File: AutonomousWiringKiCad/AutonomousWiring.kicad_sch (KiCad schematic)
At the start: 30 parts

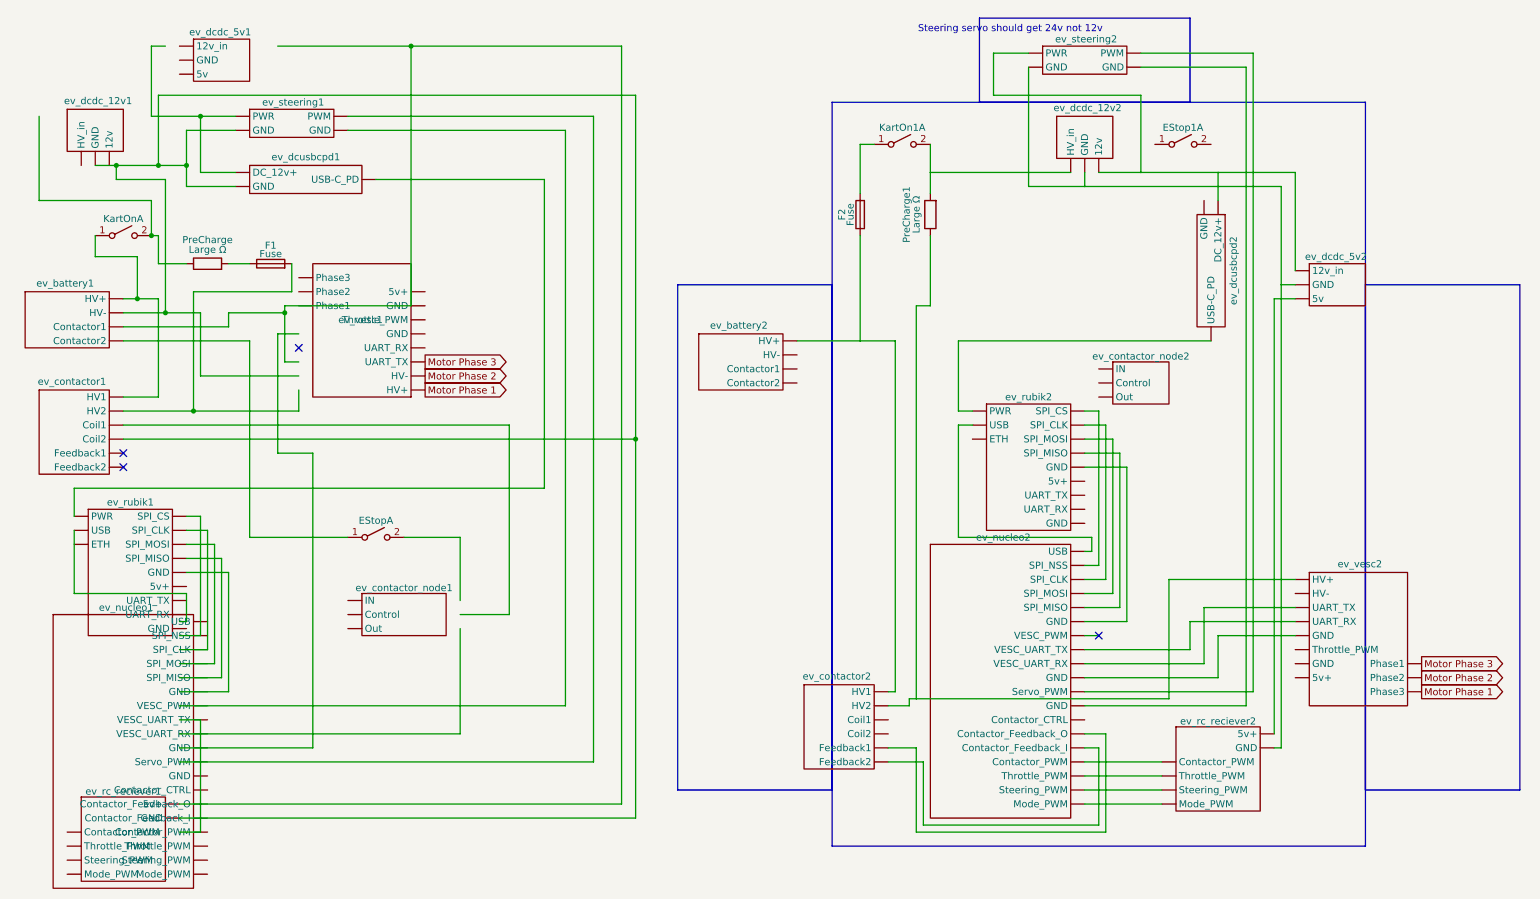
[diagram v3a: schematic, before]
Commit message: Not perfect but all wires in
- Servo needs 24v
- Missing bullet AC (24v passive PoE)
- Missing eth switch
- Missing 4 other rubiks
- Missing purely electrical remote contactor shutoff
- Don't use relay for STM set contactor
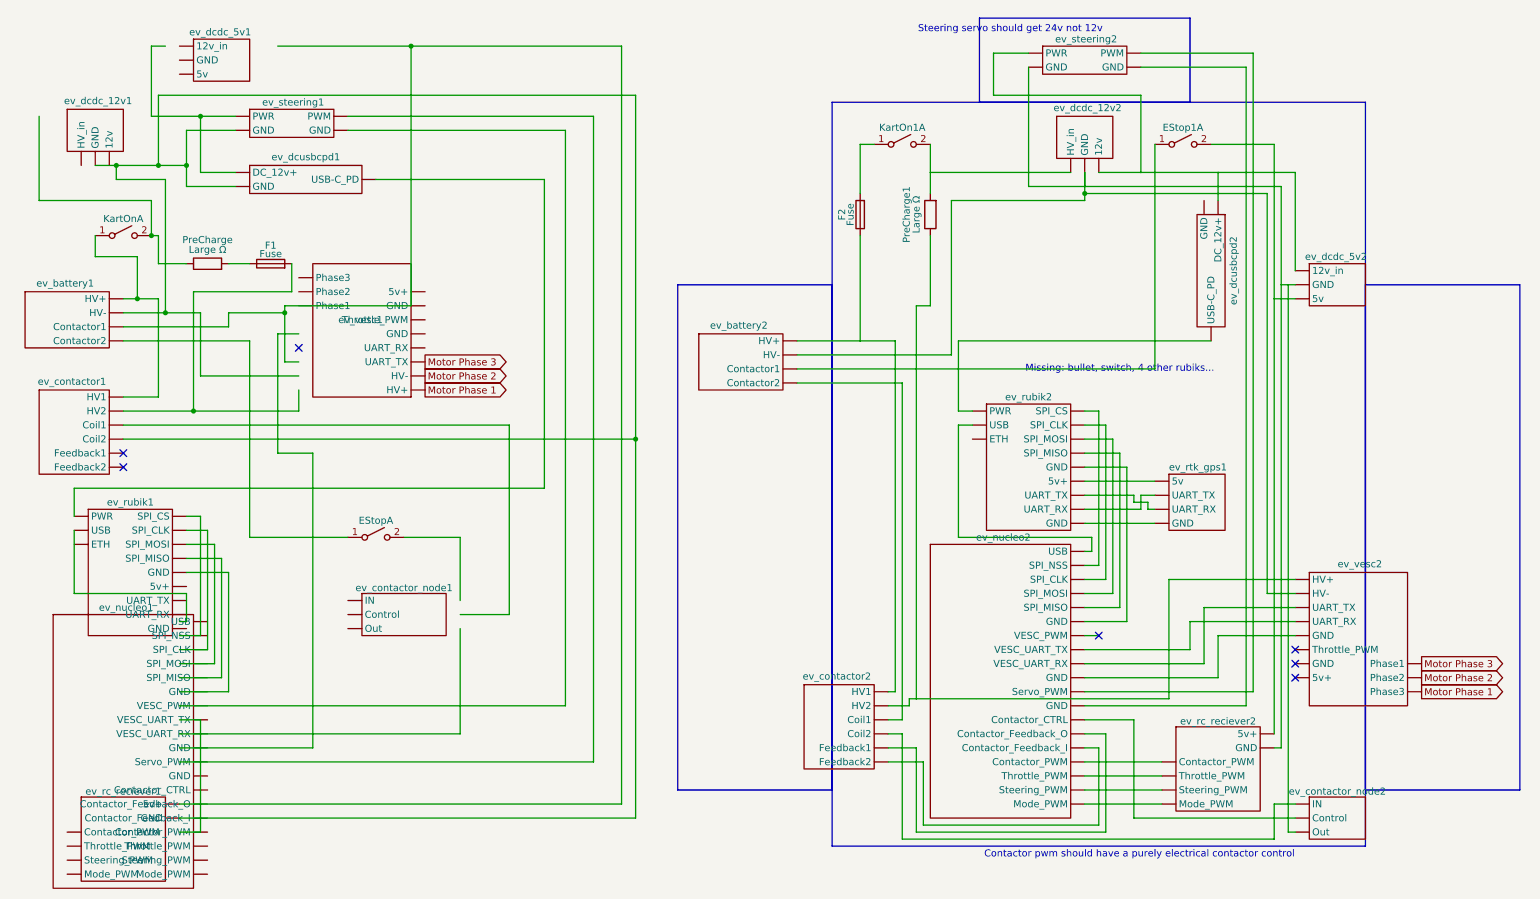
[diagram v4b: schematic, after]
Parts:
- added ev_rtk_gps1: ~, symbol ev_kart:ev_rtk_gps
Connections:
- net at ev_dcdc_12v1. (12v): now also ev_battery1. (Contactor2), ev_contactor1. (Feedback2), ev_dcusbcpd1. (USB-C_PD), ev_rc_reciever1. (GND), ev_steering1. (GND)
- net at ev_battery1. (Contactor2): now also EStop.1 (A); no longer ev_rc_reciever1. (GND)
- net at ev_nucleo2. (Mode_PWM): now also ev_vesc2. (Phase3)
- net at ev_steering2. (GND): now also ev_dcdc_12v2. (12v), ev_dcdc_5v2. (5v), ev_dcusbcpd2. (USB-C_PD); no longer ev_nucleo2. (Mode_PWM)
- net at ev_contactor2. (Feedback2): now also PreCharge1.1, ev_vesc2. (Phase3); no longer ev_nucleo2. (Mode_PWM)
- net at ev_rc_reciever2. (GND): now also EStop1.2 (B), ev_dcdc_5v2. (5v); no longer ev_nucleo2. (Mode_PWM)
- net at ev_rubik2. (GND): no longer ev_nucleo2. (Mode_PWM)
- net at ev_contactor_node2. (Out): now also ev_contactor2. (Feedback2)
- net at ev_battery2. (Contactor2): now also EStop1.1 (A)
- net at ev_steering1. (GND): now also ev_dcusbcpd1. (USB-C_PD)
- net at ev_dcusbcpd1. (USB-C_PD): now also ev_rubik1. (GND); no longer ev_steering1. (GND)
- net at ev_nucleo1. (Mode_PWM): now also ev_rubik1. (GND)
- net at ev_dcusbcpd2. (USB-C_PD): now also ev_rubik2. (GND)
- new net: ev_battery1. (Contactor2), ev_rc_reciever1. (GND)
- new net: KartOn.1 (A), ev_battery1. (Contactor2), ev_contactor1. (Feedback2)
- new net: ev_contactor_node2. (Out), ev_nucleo2. (Mode_PWM)
- new net: ev_nucleo2. (Mode_PWM), ev_steering2. (GND) (x2)
- new net: ev_contactor2. (Feedback2), ev_nucleo2. (Mode_PWM) (x2)
- new net: ev_nucleo2. (Mode_PWM), ev_rc_reciever2. (GND) (x4)
- new net: ev_nucleo2. (Mode_PWM), ev_rubik2. (GND) (x6)
- new net: ev_nucleo2. (Mode_PWM), ev_vesc2. (Phase3) (x2)
- new net: F2.1, ev_battery2. (Contactor2), ev_contactor2. (Feedback2)
- new net: ev_battery2. (Contactor2), ev_contactor_node2. (Out), ev_dcdc_12v2. (12v), ev_dcdc_5v2. (5v), ev_rc_reciever2. (GND), ev_steering2. (GND), ev_vesc2. (Phase3)
- new net: ev_battery2. (Contactor2), ev_contactor2. (Feedback2)
- new net: ev_rtk_gps1. (GND), ev_rubik2. (GND) (x4)
- now unconnected: ev_contactor1. (Feedback2), ev_contactor1. (Feedback2), ev_rc_reciever1. (GND), ev_rubik2. (GND), ev_rubik2. (GND), ev_rubik2. (GND), ev_rubik2. (GND), ev_rubik2. (GND), ev_rubik2. (GND)
- no-connect marks 4 -> 7
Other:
- note added: "Contactor pwm should have a purely electrical contactor control"
- note added: "Missing: bullet, switch, 4 other rubiks..."
- moved on the sheet: ev_contactor_node2

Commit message: Removing old draft
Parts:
- removed EStop, KartOn: SW_DPST_x2, symbol Switch:SW_DPST_x2
- removed F1: Fuse, symbol Device:Fuse
- removed PreCharge: Large Ω, symbol Device:R
- removed ev_battery1: ~, symbol ev_kart:ev_battery
- removed ev_contactor1: ~, symbol ev_kart:ev_contactor
- removed ev_contactor_node1: ~, symbol ev_kart:ev_contactor_node
- removed ev_dcdc_12v1: ~, symbol ev_kart:ev_dcdc_12v
- removed ev_dcdc_5v1: ~, symbol ev_kart:ev_dcdc_5v
- removed ev_dcusbcpd1: ~, symbol ev_kart:ev_dcusbcpd
- removed ev_nucleo1: ~, symbol ev_kart:ev_nucleo
- removed ev_rc_reciever1: ~, symbol ev_kart:ev_rc_reciever
- removed ev_rubik1: ~, symbol ev_kart:ev_rubik
- removed ev_steering1: ~, symbol ev_kart:ev_steering
- removed ev_vesc1: ~, symbol ev_kart:ev_vesc
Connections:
- net at ev_nucleo2. (Mode_PWM): now also ev_vesc2. (Phase3)
- net at ev_contactor_node2. (Out): now also ev_contactor2. (Feedback2); no longer ev_nucleo2. (Mode_PWM)
- net at ev_steering2. (GND): now also ev_dcdc_12v2. (12v), ev_dcdc_5v2. (5v), ev_dcusbcpd2. (USB-C_PD); no longer ev_nucleo2. (Mode_PWM)
- net at ev_contactor2. (Feedback2): now also PreCharge1.1, ev_vesc2. (Phase3); no longer ev_nucleo2. (Mode_PWM)
- net at ev_rc_reciever2. (GND): now also EStop1.2 (B), ev_dcdc_5v2. (5v); no longer ev_nucleo2. (Mode_PWM)
- net at ev_rubik2. (GND): no longer ev_nucleo2. (Mode_PWM)
- net at ev_battery2. (Contactor2): now also EStop1.1 (A); no longer ev_contactor2. (Feedback2)
- net at ev_dcusbcpd2. (USB-C_PD): now also ev_rubik2. (GND)
- new net: ev_contactor_node2. (Out), ev_nucleo2. (Mode_PWM)
- new net: ev_nucleo2. (Mode_PWM), ev_steering2. (GND) (x2)
- new net: ev_contactor2. (Feedback2), ev_nucleo2. (Mode_PWM) (x2)
- new net: ev_nucleo2. (Mode_PWM), ev_rc_reciever2. (GND) (x4)
- new net: ev_nucleo2. (Mode_PWM), ev_rubik2. (GND) (x6)
- new net: ev_nucleo2. (Mode_PWM), ev_vesc2. (Phase3) (x2)
- new net: F2.1, ev_battery2. (Contactor2), ev_contactor2. (Feedback2)
- new net: ev_battery2. (Contactor2), ev_contactor_node2. (Out), ev_dcdc_12v2. (12v), ev_dcdc_5v2. (5v), ev_rc_reciever2. (GND), ev_steering2. (GND), ev_vesc2. (Phase3)
- new net: ev_battery2. (Contactor2), ev_contactor2. (Feedback2)
- new net: ev_rtk_gps1. (GND), ev_rubik2. (GND) (x3)
- now unconnected: ev_rubik2. (GND), ev_rubik2. (GND), ev_rubik2. (GND), ev_rubik2. (GND), ev_rubik2. (GND), ev_rubik2. (GND), ev_rubik2. (GND), ev_rubik2. (GND), ev_rubik2. (GND)
- no-connect marks 7 -> 4
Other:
- moved on the sheet: EStop1A, F2, KartOn1A, PreCharge1, ev_battery2, ev_contactor2, ev_contactor_node2, ev_dcdc_12v2, ev_dcdc_5v2, ev_dcusbcpd2, ev_nucleo2, ev_rc_reciever2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

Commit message: Swapping 12v to 24v, placing eth setup on the side
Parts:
- removed ev_dcdc_12v2: ~, symbol ev_kart:ev_dcdc_12v
- added ev_bullet1: ~, symbol ev_kart:ev_bullet
- added ev_dcdc_24v1: ~, symbol ev_kart:ev_dcdc_24v
- added ev_eth_switch1: ~, symbol ev_kart:ev_eth_switch
- added ev_poe_adp1: ~, symbol ev_kart:ev_poe_adp
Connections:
- net at KartOn1.2 (B), PreCharge1.2: now also ev_dcdc_24v1. (24v)
- net at ev_nucleo2. (Mode_PWM): now also ev_vesc2. (Phase3)
- net at ev_contactor_node2. (Out): now also ev_contactor2. (Feedback2); no longer ev_nucleo2. (Mode_PWM)
- net at ev_contactor2. (Feedback2): now also PreCharge1.1, ev_vesc2. (Phase3); no longer ev_nucleo2. (Mode_PWM)
- net at ev_rc_reciever2. (GND): now also EStop1.2 (B), ev_dcdc_5v2. (5v); no longer ev_nucleo2. (Mode_PWM)
- net Eth Switch: now reaches ev_rubik2. (GND)
- net Eth Switch: no longer ev_nucleo2. (Mode_PWM)
- net at ev_battery2. (Contactor2): now also EStop1.1 (A); no longer ev_contactor2. (Feedback2)
- net at ev_dcusbcpd2. (USB-C_PD): now also ev_rubik2. (GND)
- new net: ev_battery2. (Contactor2), ev_contactor_node2. (Out), ev_dcdc_24v1. (24v), ev_dcdc_5v2. (5v), ev_rc_reciever2. (GND), ev_steering2. (GND), ev_vesc2. (Phase3)
- new net: ev_dcdc_24v1. (24v), ev_dcdc_5v2. (5v), ev_dcusbcpd2. (USB-C_PD), ev_steering2. (GND)
- new net: ev_contactor_node2. (Out), ev_nucleo2. (Mode_PWM)
- new net: ev_nucleo2. (Mode_PWM), ev_steering2. (GND)
- new net: ev_contactor2. (Feedback2), ev_nucleo2. (Mode_PWM) (x2)
- new net: ev_nucleo2. (Mode_PWM), ev_rc_reciever2. (GND) (x4)
- new net: ev_nucleo2. (Mode_PWM), ev_rubik2. (GND) (x6)
- new net: ev_nucleo2. (Mode_PWM), ev_vesc2. (Phase3) (x2)
- new net: F2.1, ev_battery2. (Contactor2), ev_contactor2. (Feedback2)
- new net: ev_eth_switch1. (ETH6), ev_poe_adp1. (POE_Eth) (x2)
- new net: ev_bullet1. (PoE_Eth), ev_poe_adp1. (POE_Eth)
- new net: ev_battery2. (Contactor2), ev_contactor2. (Feedback2)
- new net: ev_rtk_gps1. (GND), ev_rubik2. (GND) (x3)
- new net Rubik 1: ev_eth_switch1. (ETH6)
- new net Rubik 2: ev_eth_switch1. (ETH6)
- new net Rubik 3: ev_eth_switch1. (ETH6)
- new net Rubik 4: ev_eth_switch1. (ETH6)
- new net Rubik 5: ev_eth_switch1. (ETH6)
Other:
- note removed: "Steering servo should get 24v not 12v"

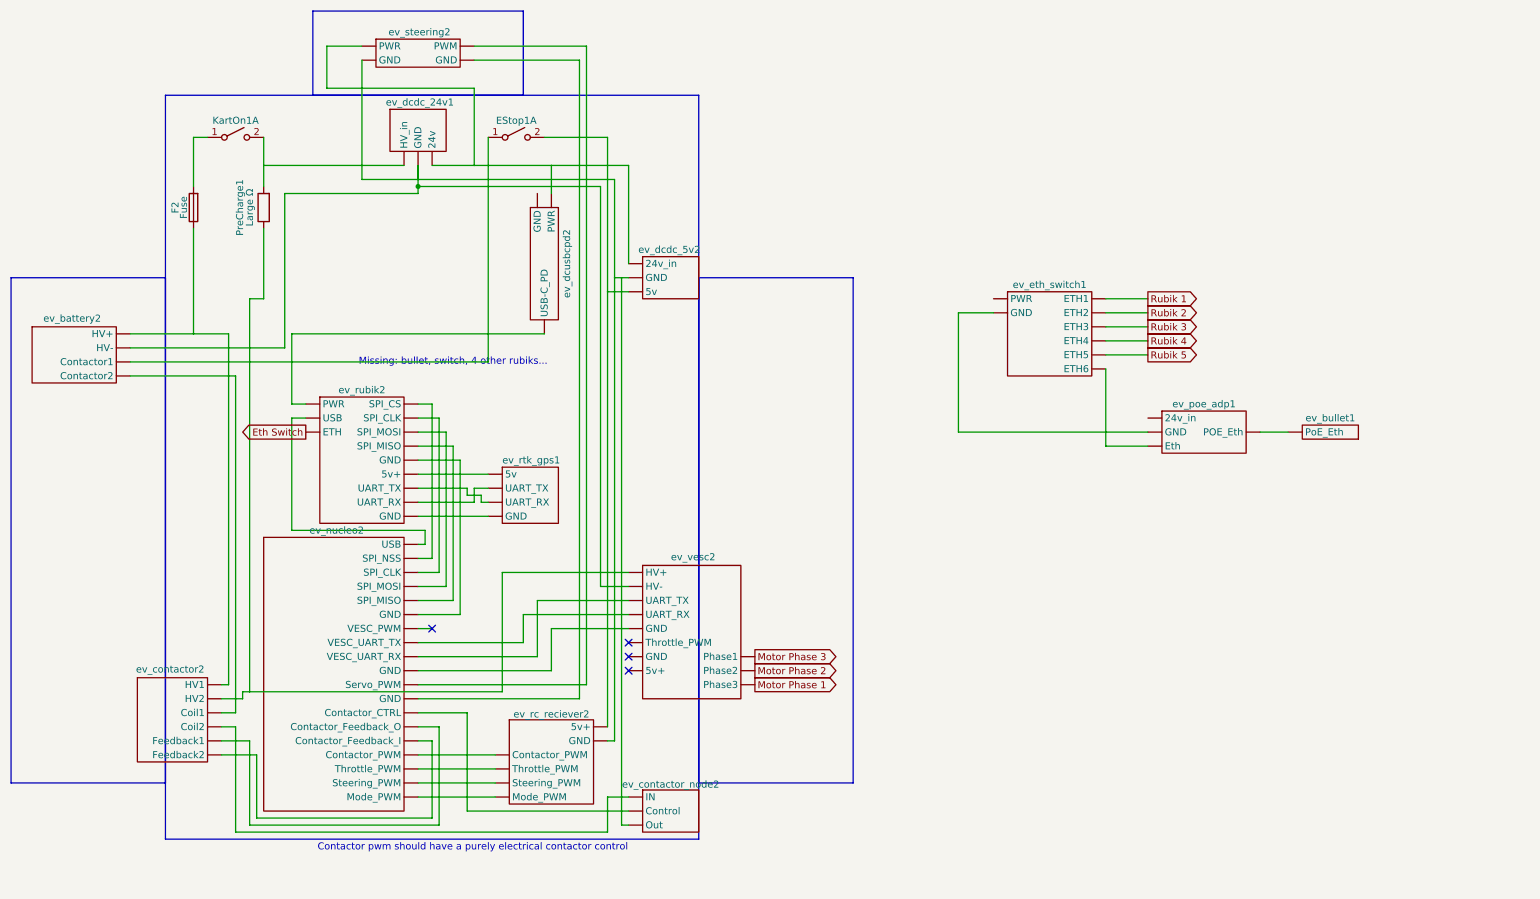
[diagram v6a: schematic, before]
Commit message: Moving eth setup into the main diagram
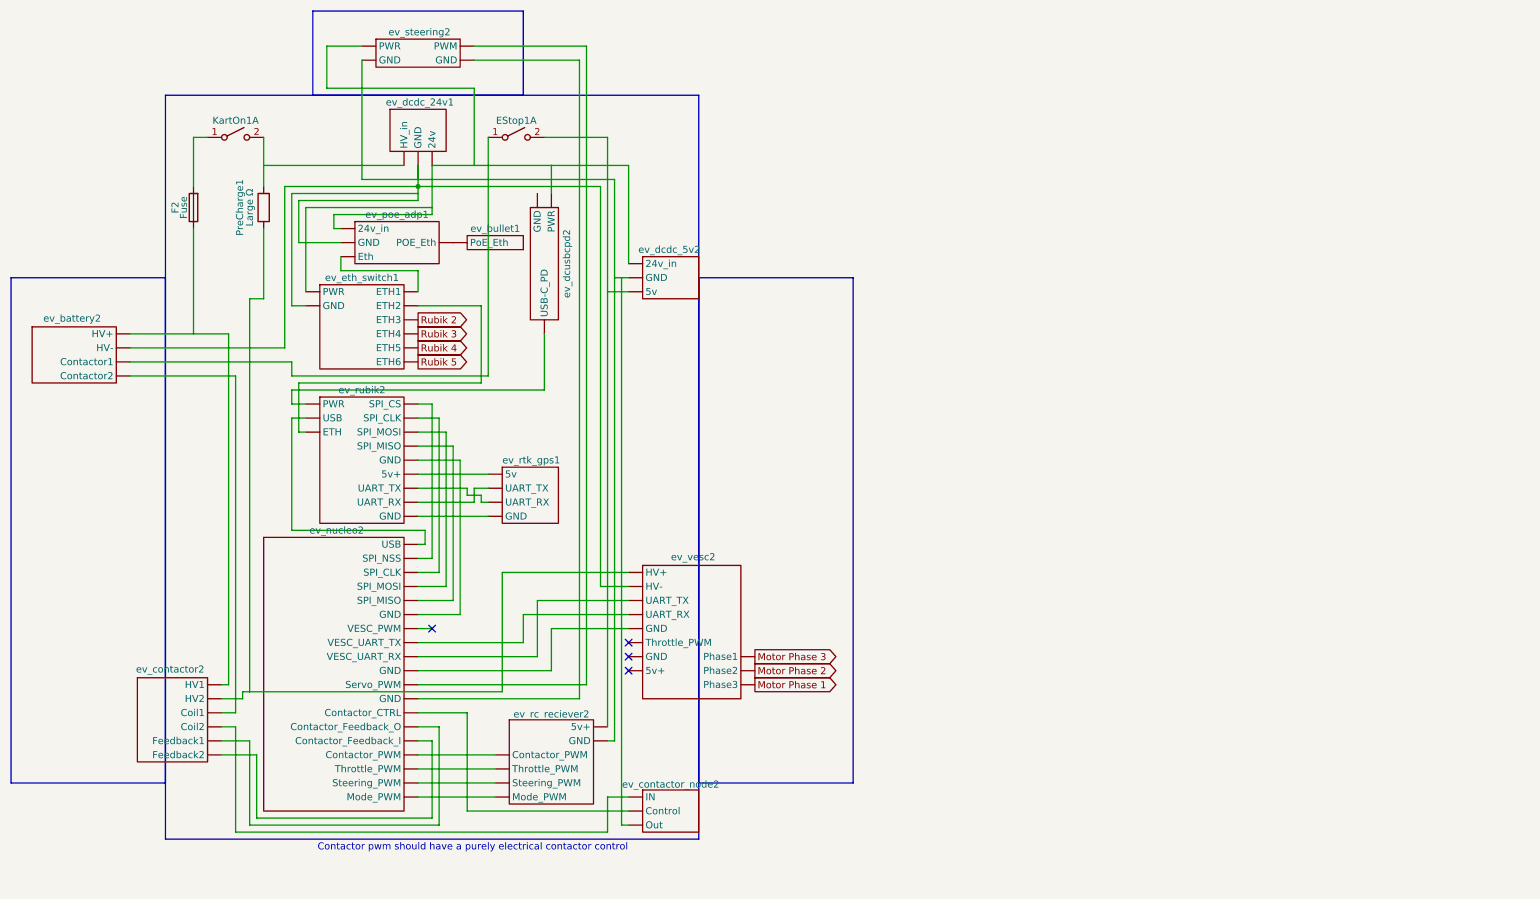
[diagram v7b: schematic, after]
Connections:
- net Eth Switch is gone; now on an unnamed net: ev_rubik2. (GND)
- net Rubik 1 is gone; now on net Rubik 5: ev_eth_switch1. (ETH6)
- net at ev_nucleo2. (Mode_PWM): now also ev_vesc2. (Phase3)
- net at ev_contactor_node2. (Out): now also ev_contactor2. (Feedback2); no longer ev_nucleo2. (Mode_PWM)
- net at ev_contactor2. (Feedback2): now also PreCharge1.1, ev_vesc2. (Phase3); no longer ev_nucleo2. (Mode_PWM)
- net at ev_rc_reciever2. (GND): now also EStop1.2 (B), ev_dcdc_5v2. (5v); no longer ev_nucleo2. (Mode_PWM)
- net at ev_rubik2. (GND): now also ev_dcusbcpd2. (USB-C_PD); no longer ev_nucleo2. (Mode_PWM)
- net at ev_poe_adp1. (POE_Eth): now also ev_bullet1. (PoE_Eth)
- net at ev_battery2. (Contactor2): now also EStop1.1 (A); no longer ev_contactor2. (Feedback2)
- new net: ev_battery2. (Contactor2), ev_contactor_node2. (Out), ev_dcdc_24v1. (24v), ev_dcdc_5v2. (5v), ev_eth_switch1. (ETH6), ev_poe_adp1. (POE_Eth), ev_rc_reciever2. (GND), ev_steering2. (GND), ev_vesc2. (Phase3)
- new net: ev_dcdc_24v1. (24v), ev_dcdc_5v2. (5v), ev_dcusbcpd2. (USB-C_PD), ev_eth_switch1. (ETH6), ev_poe_adp1. (POE_Eth), ev_steering2. (GND)
- new net: ev_contactor_node2. (Out), ev_nucleo2. (Mode_PWM)
- new net: ev_nucleo2. (Mode_PWM), ev_steering2. (GND)
- new net: ev_contactor2. (Feedback2), ev_nucleo2. (Mode_PWM) (x2)
- new net: ev_nucleo2. (Mode_PWM), ev_rc_reciever2. (GND) (x4)
- new net: ev_nucleo2. (Mode_PWM), ev_rubik2. (GND) (x6)
- new net: ev_nucleo2. (Mode_PWM), ev_vesc2. (Phase3) (x2)
- new net: F2.1, ev_battery2. (Contactor2), ev_contactor2. (Feedback2)
- new net: ev_eth_switch1. (ETH6), ev_poe_adp1. (POE_Eth)
- new net: ev_battery2. (Contactor2), ev_contactor2. (Feedback2)
- new net: ev_eth_switch1. (ETH6), ev_rubik2. (GND)
- new net: ev_rtk_gps1. (GND), ev_rubik2. (GND) (x3)
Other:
- note removed: "Missing: bullet, switch, 4 other rubiks..."
- moved on the sheet: ev_bullet1, ev_eth_switch1, ev_poe_adp1
